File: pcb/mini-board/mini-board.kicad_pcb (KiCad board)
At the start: 4 copper layers, 132.1 x 132.1 mm, 55 parts, among them J1 USB_B, J2 EXPANSION BUS, J3 SD Card Board, J4 Atmel-JTAG-10, J5 SYSTEM BUS, J8 SERIAL, SW1 SW_SPDT, SW2 RESET, SW3 NMI, U1 74AC11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

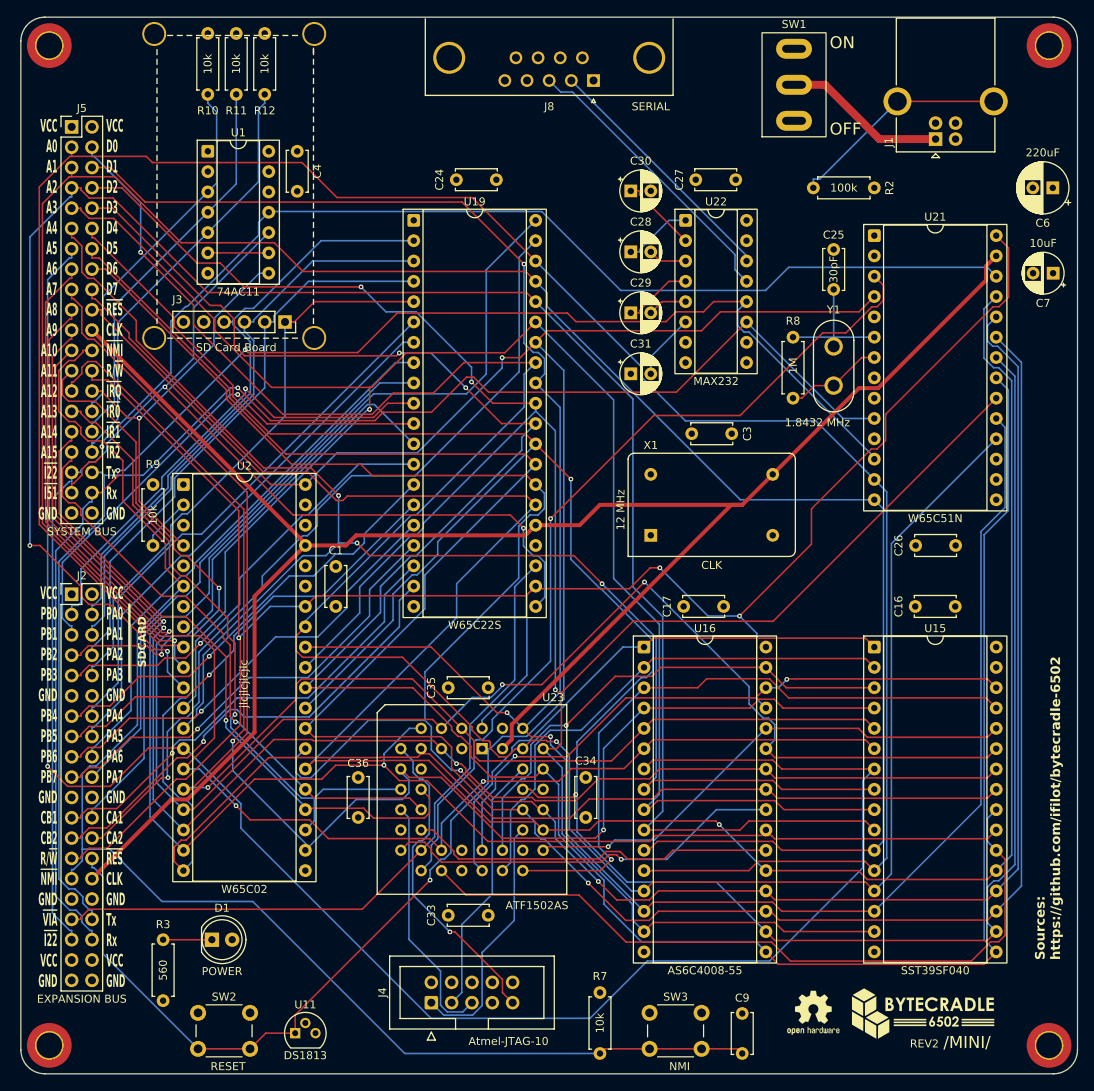
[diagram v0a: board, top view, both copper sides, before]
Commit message: Adding 10k resistor to IRQ51
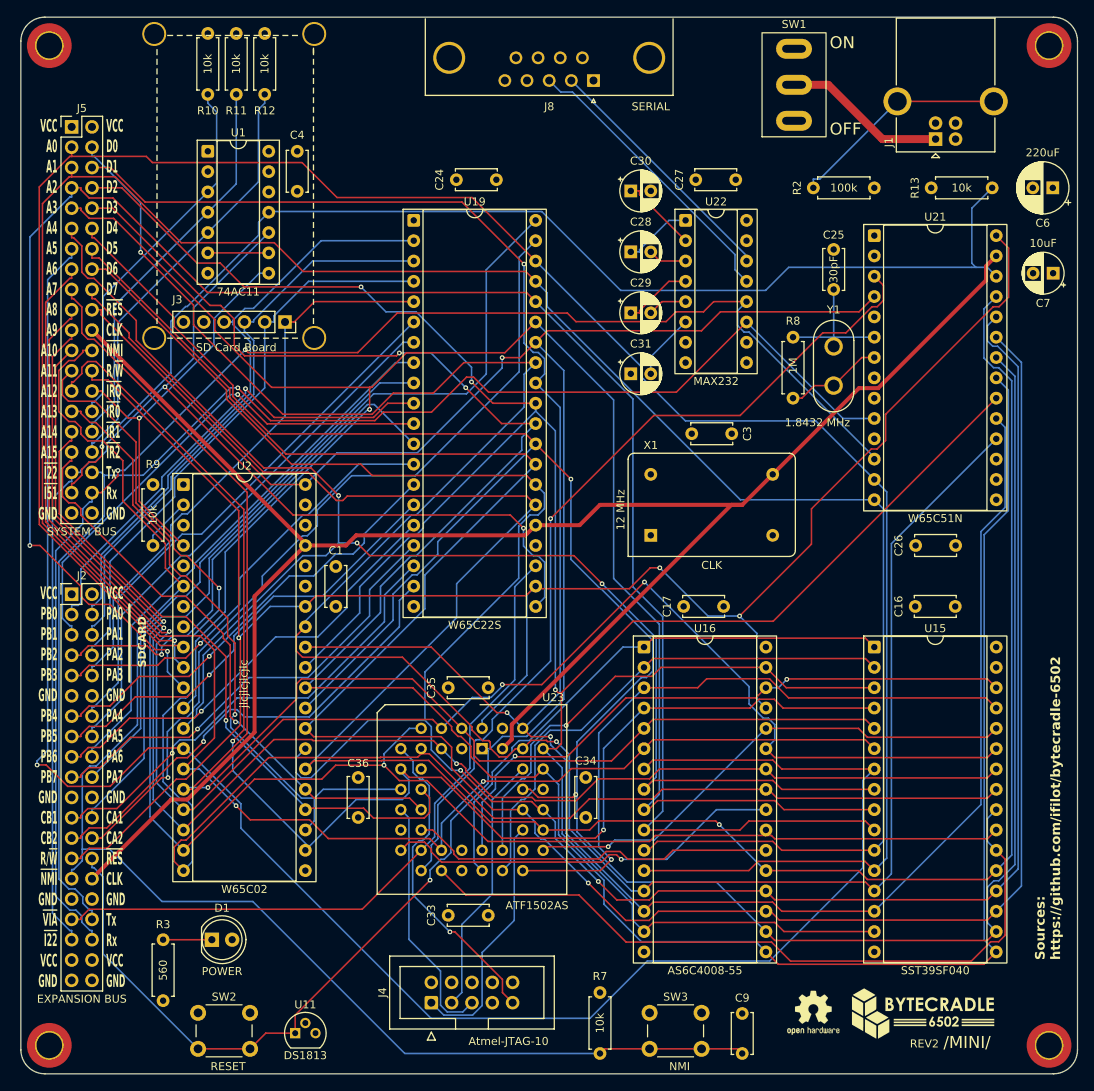
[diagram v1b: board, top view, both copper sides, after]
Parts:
- added R13: 10k, Resistor_THT:R_Axial_DIN0207_L6.3mm_D2.5mm_P7.62mm_Horizontal, F.Cu at (240.8, 46.7)
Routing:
- net ~{IRQ51}: track 142.7 -> 153.9 mm
- net A5: track 237.3 -> 239.0 mm
